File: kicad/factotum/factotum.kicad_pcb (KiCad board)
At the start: 2 copper layers, 91.4 x 99.7 mm, 156 parts, among them J1 Conn_01x06, J10 OUT3, J11 OUT5, J12 OUT7, J13 Conn_01x08_Female, J14 OUT2, J15 OUT4, J16 OUT6, J17 OUT8, J18 Conn_01x08_Male, J19 Conn_01x17_Female, J2 USART, J20 Conn_01x17_Male, J21 Conn_01x05_Male, J22 Conn_01x08_Male, J3 Conn_02x05_Odd_Even, J4 Conn_01x05_Female, J5 VOCT, J6 Conn_01x08_Female, J7 RST, J8 CLK, J9 OUT1, P1 10k, P2 10k, P3 10k, P4 10k, SW1 MODE_SW, U1 STM32F411RETx, U10 DAC128S085, U15 PCA9685PW, U2 R-78E3.3-0.5, U3 LD2981ABU33, U4 MCP6004, U5 ADC128S022, U6 LM2902, U7 LM2902, U8 M24C02-RMN, Y1 16 MHz

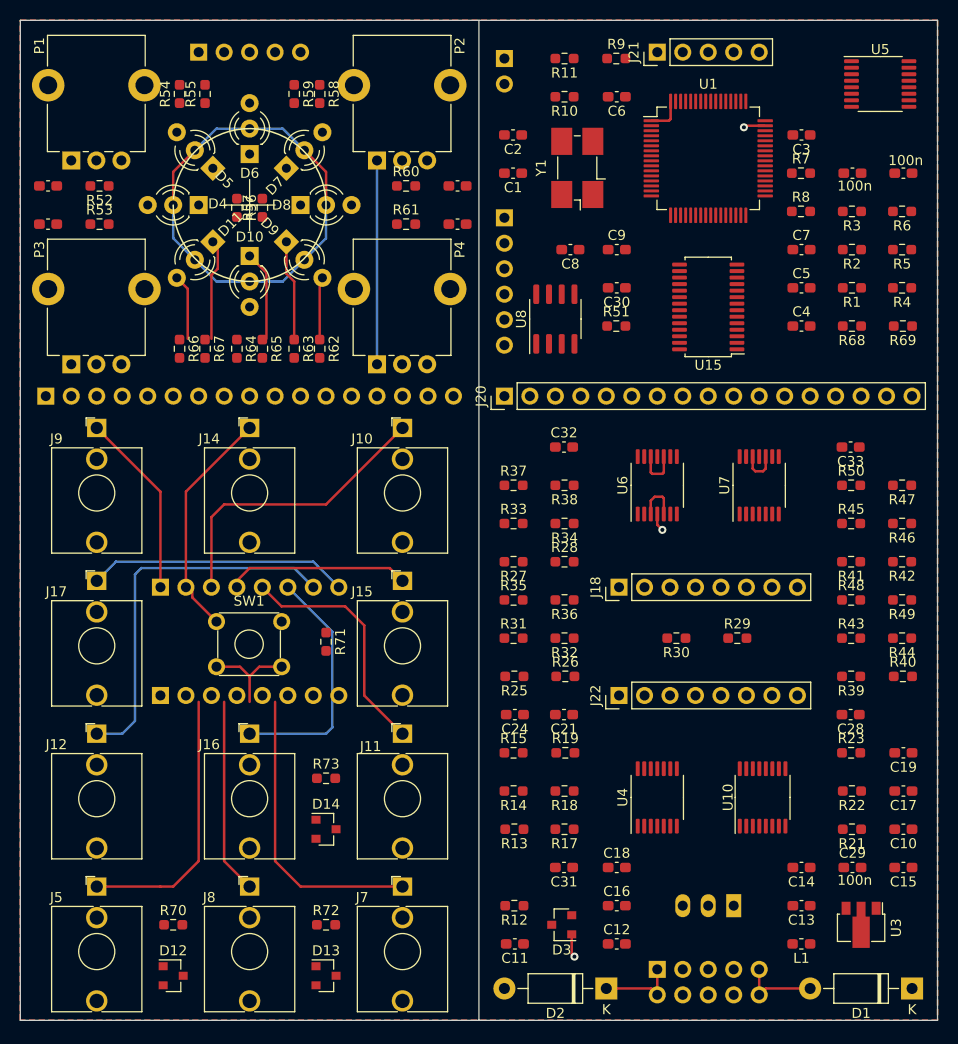
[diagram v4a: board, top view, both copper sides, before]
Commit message: working on pcd routing
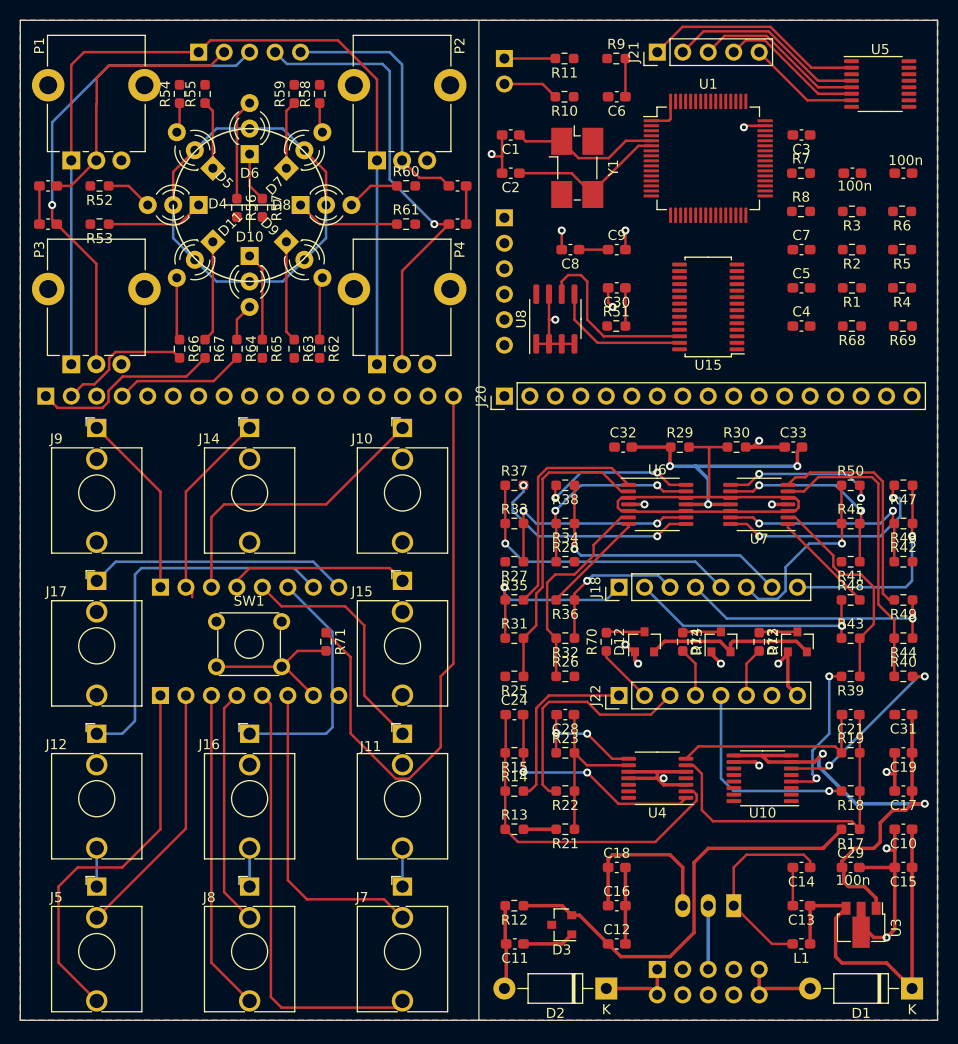
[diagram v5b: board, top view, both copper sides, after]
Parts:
- moved D12 57.6 mm to (162.6, 77.2), turned to 90 degrees
- moved D13 57.6 mm to (177.8, 77.2), turned to 90 degrees
- moved R70 51.6 mm to (158.8, 77.2), turned to 90 degrees
- moved R72 51.6 mm to (174.0, 77.2), turned to 270 degrees
- moved D14 43.6 mm to (170.2, 77.2), turned to 90 degrees
- moved R73 38.1 mm to (166.4, 77.2), turned to 270 degrees
- moved C31 37.1 mm to (188.4, 84.5)
- moved R21 28.6 mm to (154.7, 95.9)
- moved R22 28.6 mm to (154.7, 92.1)
- moved C21 28.6 mm to (183.1, 84.5)
- moved R17 28.5 mm to (183.1, 95.9)
- moved R18 28.5 mm to (183.1, 92.1)
- moved R23 28.5 mm to (154.7, 88.3)
- moved C28 28.4 mm to (154.7, 84.5)
- moved R19 28.4 mm to (183.1, 88.3)
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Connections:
- net Net-(D1-Pad2) renamed IN_POS
- net Net-(D2-Pad1) renamed IN_NEG
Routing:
- net +3.3VA: track 20.3 -> 216.7 mm, vias 0 -> 5
- net +3V3: track 54.6 -> 137.6 mm
- net T_OFF: track 0.00 -> 48.5 mm, vias 0 -> 1
- net T_SCL: track 0.00 -> 46.7 mm, vias 0 -> 1
- net -10V: track 0.00 -> 46.5 mm
- net T_RST: track 0.00 -> 44.2 mm
- net T_VOCT: track 0.00 -> 38.8 mm
- net +12V: track 0.00 -> 37.6 mm
- net GND: track 86.9 -> 124.1 mm, vias 3 -> 18
- net Net-(C24-Pad1): track 0.00 -> 34.6 mm
- net VREF: track 13.0 -> 47.1 mm
- net Net-(C21-Pad1): track 0.00 -> 33.5 mm
- net T_CLK: track 0.00 -> 32.0 mm
- net T_RST_SW: track 0.00 -> 31.4 mm
- net Net-(R25-Pad1): track 0.00 -> 30.1 mm
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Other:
- net class Power added: clearance 0.2, trace_width 0.35, via_dia 0.8, via_drill 0.4

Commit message: more work on routing
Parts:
- J19: value Conn_01x17_Female -> Conn_01x05_Male; footprint Connector_PinSocket_2.54mm:PinSocket_1x17_P2.54mm_Vertical -> Connector_PinHeader_2.54mm:PinHeader_1x05_P2.54mm_Vertical; moved to F.Cu
- J20: value Conn_01x17_Male -> Conn_01x08_Male; footprint Connector_PinHeader_2.54mm:PinHeader_1x17_P2.54mm_Vertical -> Connector_PinHeader_2.54mm:PinHeader_1x08_P2.54mm_Vertical
- J21: value Conn_01x05_Male -> Conn_01x17_Female; footprint Connector_PinHeader_2.54mm:PinHeader_1x05_P2.54mm_Vertical -> Connector_PinSocket_2.54mm:PinSocket_1x17_P2.54mm_Vertical; moved to B.Cu
- J22: value Conn_01x08_Male -> Conn_01x17_Male; footprint Connector_PinHeader_2.54mm:PinHeader_1x08_P2.54mm_Vertical -> Connector_PinHeader_2.54mm:PinHeader_1x17_P2.54mm_Vertical
- J4: value Conn_01x05_Female -> Conn_01x08_Female; footprint Connector_PinSocket_2.54mm:PinSocket_1x05_P2.54mm_Vertical -> Connector_PinSocket_2.54mm:PinSocket_1x08_P2.54mm_Vertical
- J6: value Conn_01x08_Female -> Conn_01x05_Female; footprint Connector_PinSocket_2.54mm:PinSocket_1x08_P2.54mm_Vertical -> Connector_PinSocket_2.54mm:PinSocket_1x05_P2.54mm_Vertical
- moved J19 69.9 mm to (163.8, 18.4), turned to 90 degrees
- moved J21 69.9 mm to (102.9, 52.7), turned to 270 degrees
- moved J6 64.2 mm to (118.1, 18.4)
- moved J4 53.5 mm to (114.3, 71.8)
- moved J20 32.0 mm to (160.0, 82.5)
- moved J22 32.0 mm to (148.6, 52.7)
- moved R7 19.1 mm to (197.2, 31.8)
- moved R8 19.1 mm to (197.2, 35.6)
- moved C4 11.4 mm to (178.2, 34.3)
- moved J13 10.8 mm to (114.3, 82.5)
- moved C7 7.62 mm to (178.2, 30.5)
- moved R52 3.81 mm to (108.3, 35.6)
- moved R53 3.81 mm to (108.2, 31.8)
- moved C5 3.81 mm to (178.2, 38.1)
- moved R66 2.54 mm to (118.7, 48.0)
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- renumbered D4 to D1, D2 to D10, D3 to D11, D5 to D2, D6 to D3, D7 to D4, D8 to D5, D9 to D6, D10 to D7, D11 to D8, D1 to D9
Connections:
- J13 pad 1: T_1 -> T_VOCT
- J13 pad 2: T_2 -> T_VOCT_SW
- J13 pad 3: T_3 -> T_CLK
- J13 pad 4: T_4 -> T_CLK_SW
- J13 pad 5: T_5 -> T_RST
- J13 pad 6: T_6 -> T_RST_SW
- J13 pad 7: T_7 -> T_MODE_SW
- J13 pad 8: T_8 -> GND
- J19 pad 1: G8_T -> B_FRQ
- J19 pad 2: R8_T -> B_OFF
- J19 pad 3: G7_T -> +3.3VA
- J19 pad 4: R7_T -> B_SCL
- J19 pad 5: G6_T -> B_SEL
- J20 pad 1: Net-(J20-Pad1) -> B_VOCT
- J20 pad 2: Net-(J20-Pad2) -> B_VOCT_SW
- J20 pad 3: Net-(J20-Pad3) -> B_CLK
- J20 pad 4: Net-(J20-Pad4) -> B_CLK_SW
- J20 pad 5: Net-(J20-Pad5) -> B_RST
- J20 pad 6: Net-(J20-Pad6) -> B_RST_SW
- J20 pad 7: Net-(J20-Pad7) -> B_MODE_SW
- J20 pad 8: Net-(J20-Pad8) -> GND
- J21 pad 1: +3.3VA -> G2_T
- J21 pad 2: B_FRQ -> R2_T
- J21 pad 3: B_OFF -> G1_T
- J21 pad 4: B_SCL -> R1_T
- J21 pad 5: B_SEL -> G8_T
- J22 pad 1: B_VOCT -> G2_B
- J22 pad 2: B_VOCT_SW -> R2_B
- J22 pad 3: B_CLK -> G1_B
- J22 pad 4: B_CLK_SW -> R1_B
- J22 pad 5: B_RST -> G8_B
- J22 pad 6: B_RST_SW -> R8_B
- J22 pad 7: B_MODE_SW -> G7_B
- J22 pad 8: GND -> R7_B
- J4 pad 1: +3.3VA -> T_1
- J4 pad 2: T_FRQ -> T_2
- J4 pad 3: T_OFF -> T_3
- J4 pad 4: T_SCL -> T_4
- J4 pad 5: T_SEL -> T_5
- J6 pad 1: T_VOCT -> T_FRQ
- J6 pad 2: T_VOCT_SW -> T_OFF
- J6 pad 3: T_CLK -> +3.3VA
- J6 pad 4: T_CLK_SW -> T_SCL
- J6 pad 5: T_RST -> T_SEL
- U15 pad 10: Net-(J20-Pad12) -> R3_B
- U15 pad 11: Net-(J20-Pad11) -> G3_B
- U15 pad 12: Net-(J20-Pad10) -> R4_B
- U15 pad 13: Net-(J20-Pad9) -> G4_B
- U15 pad 15: Net-(J20-Pad8) -> R5_B
- U15 pad 16: Net-(J20-Pad7) -> G5_B
- U15 pad 17: Net-(J20-Pad6) -> R6_B
- U15 pad 18: Net-(J20-Pad5) -> G6_B
- U15 pad 19: Net-(J20-Pad4) -> R7_B
- U15 pad 20: Net-(J20-Pad3) -> G7_B
- U15 pad 21: Net-(J20-Pad2) -> R8_B
- U15 pad 22: Net-(J20-Pad1) -> G8_B
- U15 pad 6: Net-(J20-Pad16) -> R1_B
- U15 pad 7: Net-(J20-Pad15) -> G1_B
- U15 pad 8: Net-(J20-Pad14) -> R2_B
- U15 pad 9: Net-(J20-Pad13) -> G2_B
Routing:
- net +3V3: track 137.6 -> 340.6 mm, vias 0 -> 5
- net +3.3VA: track 216.7 -> 325.3 mm, vias 5 -> 9
- net SPI2_SCLK: track 0.00 -> 83.1 mm, vias 0 -> 2
- net SPI2_MOSI: track 0.00 -> 71.7 mm, vias 0 -> 2
- net DAC_SYNC: track 0.00 -> 71.2 mm, vias 0 -> 2
- net SPI2_MISO: track 0.00 -> 68.4 mm, vias 0 -> 2
- net DAC5: track 0.00 -> 54.5 mm
- net GND: track 124.1 -> 170.1 mm, vias 18 -> 20
- net G2_T: track 0.00 -> 42.8 mm, vias 0 -> 1
- net R3_T: track 0.00 -> 42.6 mm, vias 0 -> 1
- net G2_B: track 0.00 -> 41.5 mm
- net R4_T: track 0.00 -> 38.2 mm, vias 0 -> 1
- net G3_T: track 0.00 -> 37.9 mm, vias 0 -> 1
- net G4_T: track 0.00 -> 37.8 mm, vias 0 -> 1
- net R2_T: track 0.00 -> 36.7 mm, vias 0 -> 1
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
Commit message: finished routing
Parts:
- moved R7 23.6 mm to (178.2, 45.7)
- moved R8 20.1 mm to (178.2, 41.9)
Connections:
- U1 pad 14: B_MODE_SW -> Net-(U1-Pad14)
- U1 pad 50: Net-(U1-Pad50) -> B_MODE_SW
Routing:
- net ADC_RST: track 20.1 -> 178.5 mm, vias 0 -> 2
- net ADC_CLK: track 12.1 -> 170.3 mm, vias 2 -> 4
- net ADC_VOCT: track 23.5 -> 173.8 mm, vias 2 -> 4
- net GND: track 170.1 -> 273.9 mm, vias 20 -> 39
- net +3.3VA: track 325.3 -> 425.4 mm, vias 9 -> 15
- net B_RST_SW: track 4.96 -> 98.3 mm, vias 0 -> 1
- net B_CLK_SW: track 4.96 -> 96.4 mm, vias 0 -> 1
- net B_MODE_SW: track 0.00 -> 86.8 mm, vias 0 -> 3
- net B_VOCT_SW: track 6.02 -> 83.6 mm, vias 0 -> 2
- net NSRT: track 0.00 -> 62.3 mm, vias 0 -> 2
- net I2C1_SDA: track 15.7 -> 70.2 mm, vias 2 -> 6
- net DAC1: track 0.00 -> 50.7 mm, vias 0 -> 4
- net I2C1_SCL: track 16.7 -> 65.3 mm, vias 2 -> 4
- net SWDIO: track 0.00 -> 47.4 mm, vias 0 -> 2
- net SWO: track 0.00 -> 46.7 mm, vias 0 -> 2
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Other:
- board text added: "+12"
- board text added: "-12"
- board text added: "3v3"
- board text added: "GND"
- board text added: "NSRT"
- board text added: "RX"
- board text added: "SWCLK"
- board text added: "SWDIO"
- board text added: "SWO"
- board text added: "TX"
